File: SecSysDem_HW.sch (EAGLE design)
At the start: 49 parts, among them IC1 L7805 5V, Q1 2N3904, T1 MOSFET_NCHANNEL_ENHANCEMENT2N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, T2 MOSFET_NCHANNEL_ENHANCEMENT2N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, T3 MOSFET_NCHANNEL_ENHANCEMENT2N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, U1 XPLAINED_MINI_PINOUT, U2 PCF8574_IO_EXPANDER, U4 FT24C512A, U5 MCP4901-E/SN, X1 C-GRID-06-70553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

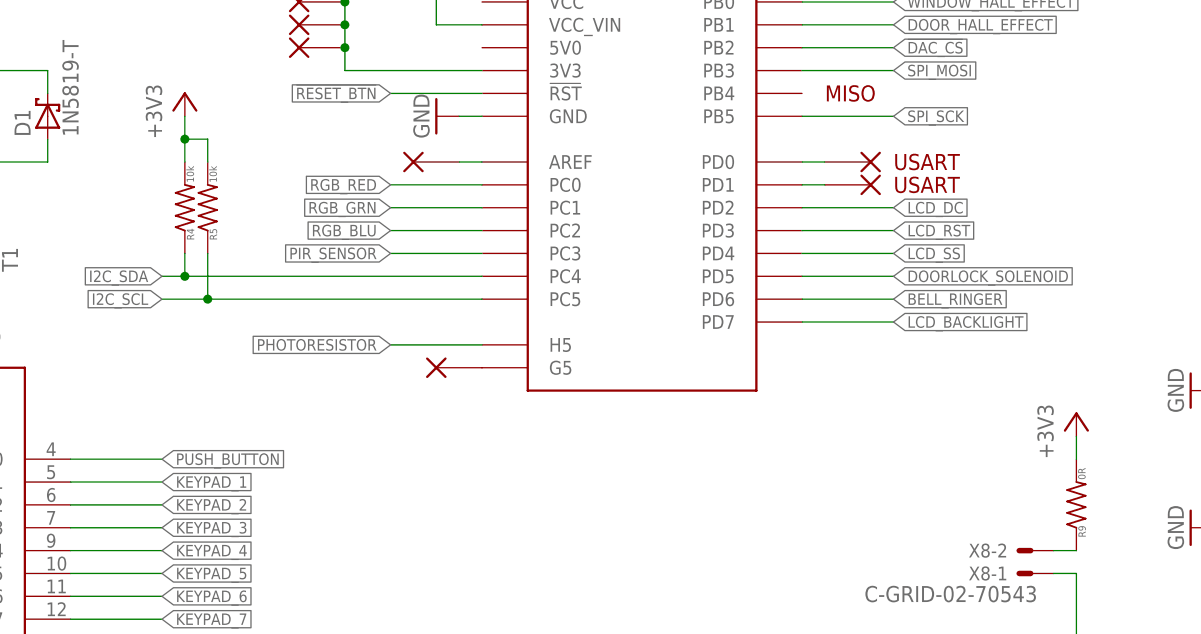
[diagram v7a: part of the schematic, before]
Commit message: Continued PCB layout. Moved some pin options.
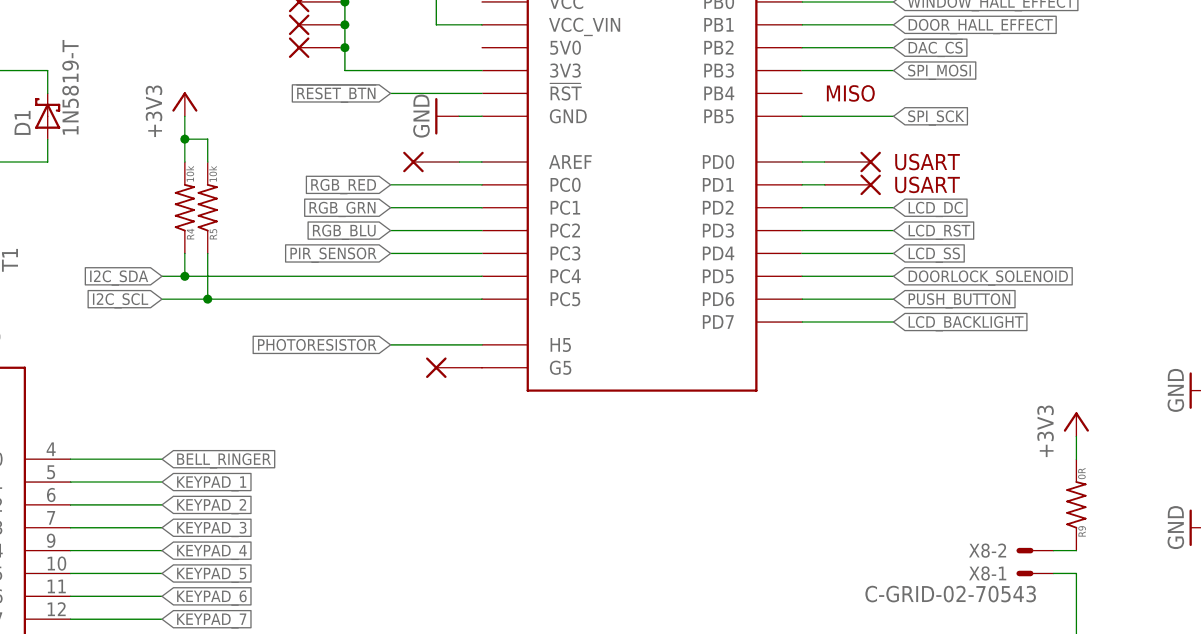
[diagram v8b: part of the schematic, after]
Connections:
- net BELL_RINGER: now also U2.P0; no longer U1.PD6
- net PUSH_BUTTON: now also U1.PD6; no longer U2.P0
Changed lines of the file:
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@@
 <net name="PUSH_BUTTON" class="0">
 <segment>
-<wire x1="60.96" y1="48.26" x2="71.12" y2="48.26" width="0.1524" layer="91"/>
-<label x="71.12" y="48.26" size="1.27" layer="95" xref="yes"/>
-<pinref part="U2" gate="G$1" pin="P0"/>
+<wire x1="142.24" y1="66.04" x2="152.4" y2="66.04" width="0.1524" layer="91"/>
+<label x="152.4" y="66.04" size="1.27" layer="95" xref="yes"/>
+<pinref part="U1" gate="G$1" pin="PD6"/>
 </segment>
 <segment>
@@
 <net name="BELL_RINGER" class="0">
 <segment>
-<wire x1="142.24" y1="66.04" x2="152.4" y2="66.04" width="0.1524" layer="91"/>
-<label x="152.4" y="66.04" size="1.27" layer="95" xref="yes"/>
-<pinref part="U1" gate="G$1" pin="PD6"/>
+<wire x1="60.96" y1="48.26" x2="71.12" y2="48.26" width="0.1524" layer="91"/>
+<label x="71.12" y="48.26" size="1.27" layer="95" xref="yes"/>
+<pinref part="U2" gate="G$1" pin="P0"/>
 </segment>
 <segment>
@@
 <pinref part="U1" gate="G$1" pin="PD0"/>
 <pinref part="V3" gate="G$1" pin="P$1"/>
-<wire x1="144.78" y1="81.28" x2="142.24" y2="81.28" width="0.1524" layer="91"/>
+<wire x1="142.24" y1="81.28" x2="144.78" y2="81.28" width="0.1524" layer="91"/>
 </segment>
 </net>
@@
 <pinref part="U1" gate="G$1" pin="PD1"/>
 <pinref part="V4" gate="G$1" pin="P$1"/>
-<wire x1="144.78" y1="78.74" x2="142.24" y2="78.74" width="0.1524" layer="91"/>
-</segment>
-</net>
+<wire x1="142.24" y1="78.74" x2="144.78" y2="78.74" width="0.1524" layer="91"/>
+</segment>
+</net>
